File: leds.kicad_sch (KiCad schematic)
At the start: 23 parts, among them Q1 BSS138

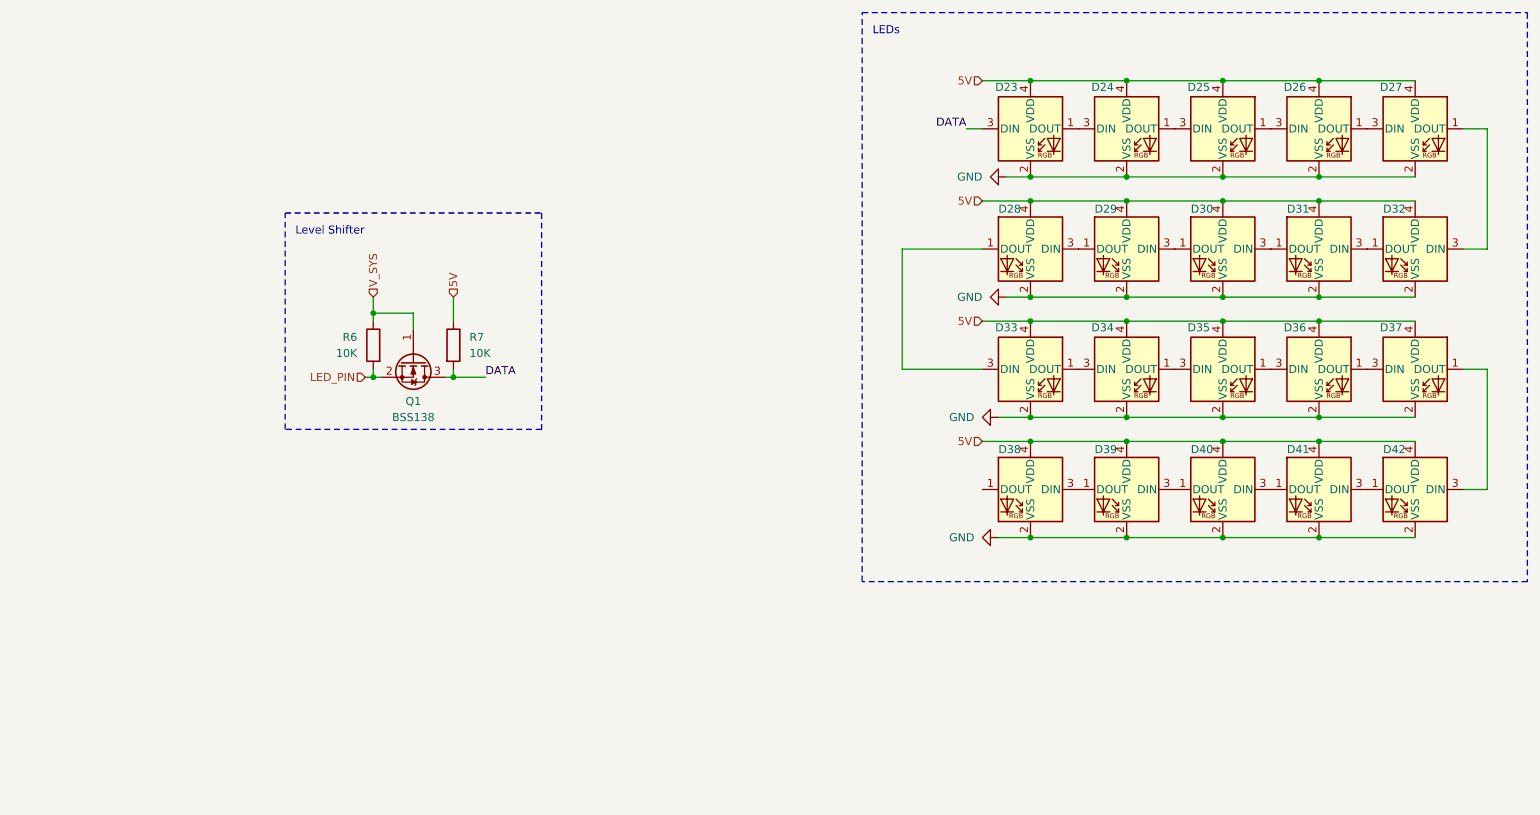
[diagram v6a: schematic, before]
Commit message: finished power circuit
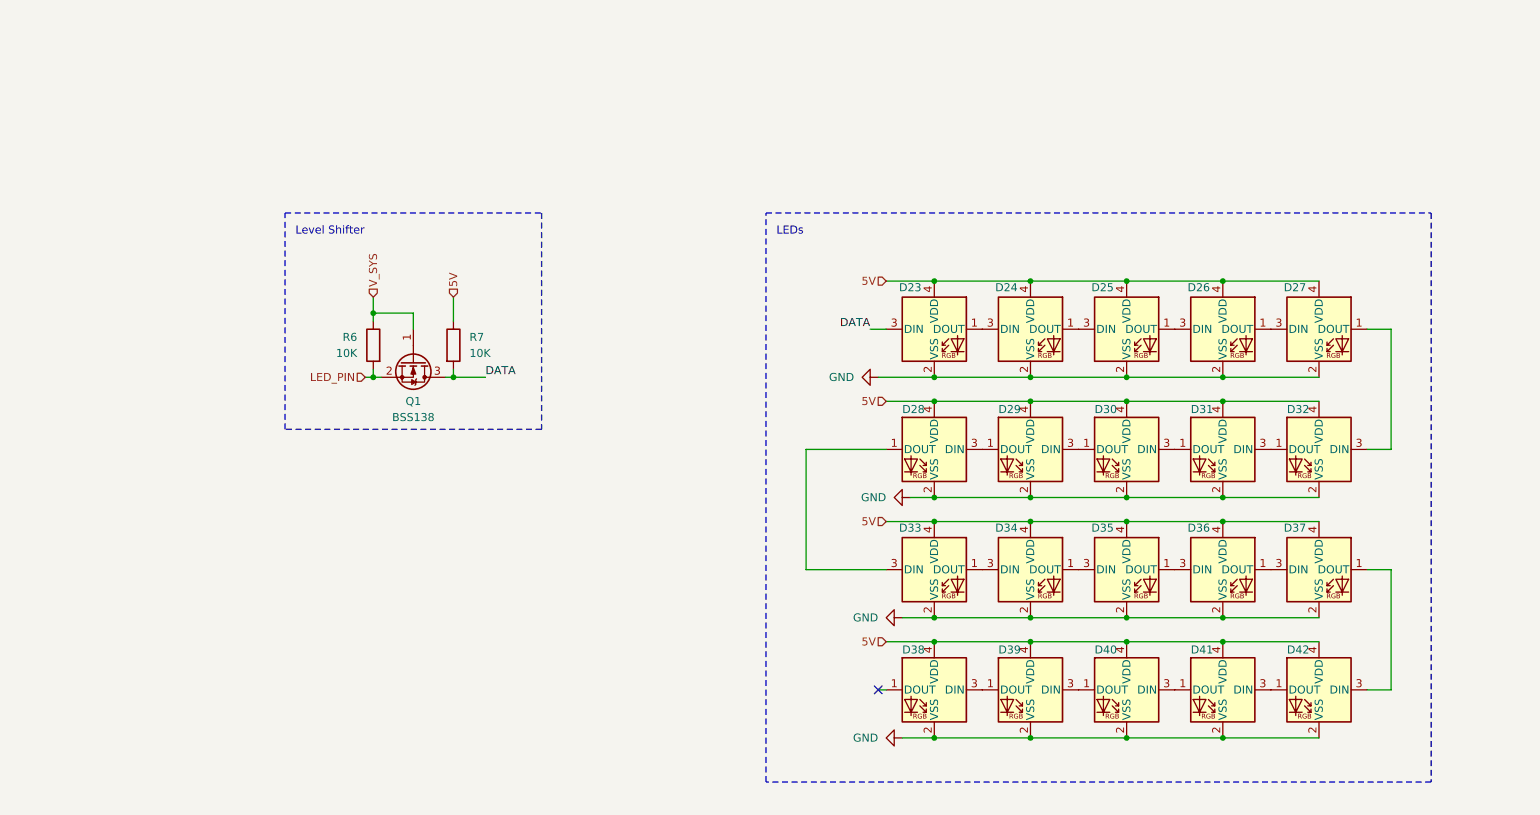
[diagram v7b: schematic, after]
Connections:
- no-connect marks 0 -> 1
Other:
- moved on the sheet: D23, D24, D25, D26, D27, D28, D29, D30, D31, D32, D33, D34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
